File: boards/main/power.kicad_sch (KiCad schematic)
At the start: 19 parts, among them Q1 DMG3415U, U3 RT9080-33GJ5, U4 MCP73831T-2ACI_OT, U5 MAX17048G_T10

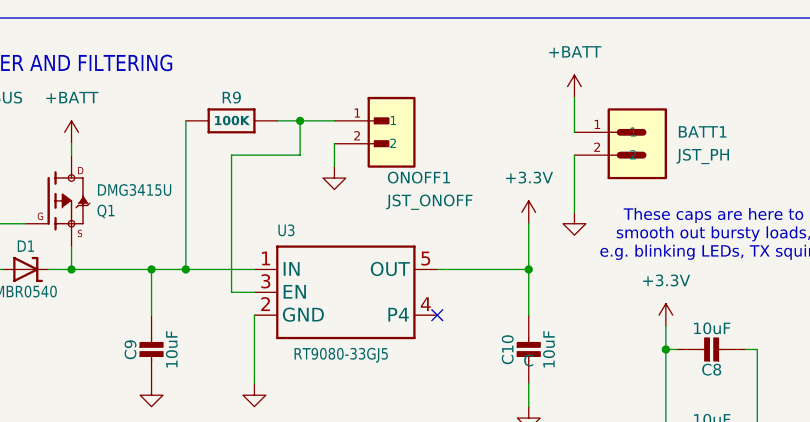
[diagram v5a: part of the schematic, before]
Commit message: Ditch the JST for the buttons, power switch, and haptic motor. Just solder direct
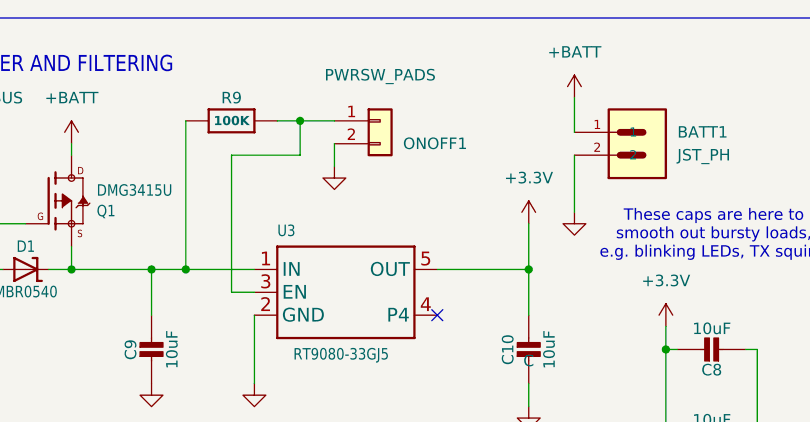
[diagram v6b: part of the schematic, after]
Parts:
- removed ONOFF1: JST_ONOFF, symbol smart_compass_main:SM02B-GHS-TB
- added ONOFF1: PWRSW_PADS, Connector_Wire:SolderWire-0.127sqmm_1x02_P3.7mm_D0.48mm_OD1mm_Relief, symbol Connector_Generic:Conn_01x02
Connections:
- net GND: now also ONOFF1.2 (Pin_2)
- net at R9.2, U3.3 (EN): now also ONOFF1.1 (Pin_1)
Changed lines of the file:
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@@
 	)
 	(symbol
-		(lib_id "smart_compass_main:SM02B-GHS-TB")
-		(at 203.2 41.91 0)
-		(unit 1)
-		(body_style 1)
-		(exclude_from_sim no)
-		(in_bom yes)
-		(on_board yes)
-		(in_pos_files yes)
-		(dnp no)
-		(property "Reference" "ONOFF1"
-			(at 198.882 45.72 0)
-			(show_name no)
-			(do_not_autoplace no)
-			(effects
-				(font
-					(size 1.27 1.27)
-				)
-				(justify left)
-			)
-		)
-		(property "Value" "JST_ONOFF"
-			(at 198.882 48.26 0)
-			(show_name no)
-			(do_not_autoplace no)
-			(effects
-				(font
-					(size 1.27 1.27)
-				)
-				(justify left)
-			)
-		)
-		(property "Footprint" ""
-			(at 203.2 41.91 0)
-			(hide yes)
-			(show_name no)
-			(do_not_autoplace no)
-			(effects
-				(font
-					(size 1.27 1.27)
-				)
-				(justify bottom)
-			)
-		)
-		(property "Datasheet" "https://www.jst-mfg.com/product/pdf/eng/eGH.pdf"
-			(at 203.2 41.91 0)
-			(hide yes)
-			(show_name no)
-			(do_not_autoplace no)
-			(effects
-				(font
-					(size 1.27 1.27)
-				)
-			)
-		)
-		(property "Description" "Connector Header Surface Mount, Right Angle 2 position 0.049 (1.25mm)"
-			(at 203.2 41.91 0)
-			(hide yes)
-			(show_name no)
-			(do_not_autoplace no)
-			(effects
-				(font
-					(size 1.27 1.27)
-				)
-				(justify bottom)
-			)
-		)
-		(property "MF" "JST Sales"
-			(at 203.2 41.91 0)
-			(hide yes)
-			(show_name no)
-			(do_not_autoplace no)
-			(effects
-				(font
-					(size 1.27 1.27)
-				)
-				(justify bottom)
-			)
-		)
-		(property "MP" "SM02B-GHS-TB"
-			(at 203.2 41.91 0)
-			(hide yes)
-			(show_name no)
-			(do_not_autoplace no)
-			(effects
-				(font
-					(size 1.27 1.27)
-				)
-				(justify bottom)
-			)
-		)
-		(property "MANUFACTURER" "JST"
-			(at 203.2 41.91 0)
-			(hide yes)
-			(show_name no)
-			(do_not_autoplace no)
-			(effects
-				(font
-					(size 1.27 1.27)
-				)
-				(justify bottom)
-			)
-		)
-		(property "MPN" "SM02B-GHS-TB"
-			(at 203.2 41.91 0)
-			(hide yes)
-			(show_name no)
-			(do_not_autoplace no)
-			(effects
-				(font
-					(size 1.27 1.27)
-				)
-			)
-		)
-		(property "PRICE" "0.26"
-			(at 203.2 41.91 0)
-			(hide yes)
-			(show_name no)
-			(do_not_autoplace no)
-			(effects
-				(font
-					(size 1.27 1.27)
-				)
-			)
-		)
-		(property "DigiKey_Part_Number" "455-1564-1-ND"
-			(at 203.2 41.91 0)
-			(hide yes)
-			(show_name no)
-			(do_not_autoplace no)
-			(effects
-				(font
-					(size 1.27 1.27)
-				)
-				(justify bottom)
-			)
-		)
-		(property "MAXIMUM_PACKAGE_HIEGHT" ""
-			(at 203.2 41.91 0)
-			(hide yes)
-			(show_name no)
-			(do_not_autoplace no)
-			(effects
-				(font
-					(size 1.27 1.27)
-				)
-			)
-		)
-		(property "Manufacturer" "JST Sales America Inc."
-			(at 203.2 41.91 0)
-			(hide yes)
-			(show_name no)
-			(do_not_autoplace no)
-			(effects
-				(font
-					(size 1.27 1.27)
-				)
-			)
-		)
-		(property "DigiKey_PN" "455-1564-1-ND"
-			(at 203.2 41.91 0)
-			(hide yes)
-			(show_name no)
-			(do_not_autoplace no)
-			(effects
-				(font
-					(size 1.27 1.27)
-				)
-			)
-		)
-		(pin "2"
-		)
-		(pin "1"
-		)
-		(instances
-			(project "SmartCompass"
-				(path "/0c161f28-8075-4403-a867-35208f463636/44fc6246-5945-463a-870f-e1f278c176e3"
-					(reference "ONOFF1")
-					(unit 1)
-				)
-			)
-		)
-	)
-	(symbol
 		(lib_id "power:+BATT")
 		(at 93.98 52.07 0)
@@
 					(unit 1)
 				)
+			)
+		)
+	)
+	(symbol
+		(lib_id "Connector_Generic:Conn_01x02")
+		(at 198.12 39.37 0)
+		(unit 1)
+		(body_style 1)
+		(exclude_from_sim no)
+		(in_bom yes)
+		(on_board yes)
+		(in_pos_files yes)
+		(dnp no)
+		(property "Reference" "ONOFF1"
+			(at 200.66 41.91 0)
+			(show_name no)
+			(do_not_autoplace no)
+			(effects
+				(font
+					(size 1.27 1.27)
+				)
+				(justify left)
+			)
+		)
+		(property "Value" "PWRSW_PADS"
+			(at 198.12 34.29 0)
+			(show_name no)
+			(do_not_autoplace no)
+			(effects
+				(font
+					(size 1.27 1.27)
+				)
+			)
+		)
+		(property "Footprint" "Connector_Wire:SolderWire-0.127sqmm_1x02_P3.7mm_D0.48mm_OD1mm_Relief"
+			(at 198.12 39.37 0)
+			(hide yes)
+			(show_name no)
+			(do_not_autoplace no)
+			(effects
+				(font
+					(size 1.27 1.27)
+				)
+			)
+		)
+		(property "Datasheet" ""
+			(at 198.12 39.37 0)
+			(hide yes)
+			(show_name no)
+			(do_not_autoplace no)
+			(effects
+				(font
+					(size 1.27 1.27)
+				)
+			)
+		)
+		(property "Description" "Soldered wire pads with feed-through strain relief, 2 conductors - case power switch"
+			(at 198.12 39.37 0)
+			(hide yes)
+			(show_name no)
+			(do_not_autoplace no)
+			(effects
+				(font
+					(size 1.27 1.27)
+				)
+			)
+		)
+		(property "MF" "JST Sales"
+			(at 198.12 39.37 0)
+			(hide yes)
+			(show_name no)
+			(do_not_autoplace no)
+			(effects
+				(font
+					(size 1.27 1.27)
+				)
+			)
+		)
+		(property "MP" "SM02B-GHS-TB"
+			(at 198.12 39.37 0)
+			(hide yes)
+			(show_name no)
+			(do_not_autoplace no)
+			(effects
+				(font
+					(size 1.27 1.27)
+				)
+			)
+		)
+		(property "MANUFACTURER" "JST"
+			(at 198.12 39.37 0)
+			(hide yes)
+			(show_name no)
+			(do_not_autoplace no)
+			(effects
+				(font
+					(size 1.27 1.27)
+				)
+			)
+		)
+		(property "MPN" "SM02B-GHS-TB"
+			(at 198.12 39.37 0)
+			(hide yes)
+			(show_name no)
+			(do_not_autoplace no)
+			(effects
+				(font
+					(size 1.27 1.27)
+				)
+			)
+		)
+		(property "DigiKey_Part_Number" "455-1564-1-ND"
+			(at 198.12 39.37 0)
+			(hide yes)
+			(show_name no)
+			(do_not_autoplace no)
+			(effects
+				(font
+					(size 1.27 1.27)
+				)
+			)
+		)
+		(property "MAXIMUM_PACKAGE_HIEGHT" ""
+			(at 198.12 39.37 0)
+			(hide yes)
+			(show_name no)
+			(do_not_autoplace no)
+			(effects
+				(font
+					(size 1.27 1.27)
+				)
+			)
+		)
+		(property "Manufacturer" "JST Sales America Inc."
+			(at 198.12 39.37 0)
+			(hide yes)
+			(show_name no)
+			(do_not_autoplace no)
+			(effects
+				(font
+					(size 1.27 1.27)
+				)
+			)
+		)
+		(property "DigiKey_PN" "455-1564-1-ND"
+			(at 198.12 39.37 0)
+			(hide yes)
+			(show_name no)
+			(do_not_autoplace no)
+			(effects
+				(font
+					(size 1.27 1.27)
+				)
+			)
+		)
+		(property "PRICE" "0.26"
+			(at 198.12 39.37 0)
+			(hide yes)
+			(show_name no)
+			(do_not_autoplace no)
+			(effects
+				(font
+					(size 1.27 1.27)
+				)
+			)
+		)
+		(pin "1"
+		)
+		(pin "2"
+		)
+		(instances
+			(project "SmartCompass"
+				(path "/0c161f28-8075-4403-a867-35208f463636/44fc6246-5945-463a-870f-e1f278c176e3"
+					(reference "ONOFF1")
+					(unit 1)
+				)

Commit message: DMG3415U was superceeded - swap it out and update the docs. Also add another bulk cap to the haptic driver to accommodate the new motor
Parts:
- Q1: value DMG3415U -> DMP2045U; footprint (none) -> Package_TO_SOT_SMD:SOT-23; DigiKey_PN DMG3415UDICT-ND -> DMP2045U-7DICT-ND; MPN DMG3415U-7 -> DMP2045U-7; PRICE 0.48 -> 0.44; Sourcing_Note (none) -> P-channel power mux between the battery and the LDO input: 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
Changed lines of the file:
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@@
 			)
 		)
-		(property "Value" "DMG3415U"
+		(property "Value" "DMP2045U"
 			(at 166.624 46.355 0)
 			(show_name no)
@@
 			)
 		)
-		(property "Footprint" ""
+		(property "Footprint" "Package_TO_SOT_SMD:SOT-23"
 			(at 163.83 48.26 0)
 			(hide yes)
@@
 			)
 		)
-		(property "Datasheet" "https://mm.digikey.com/Volume0/opasdata/d220001/medias/docus/416/DMG3415U.pdf"
+		(property "Datasheet" "https://www.diodes.com/assets/Datasheets/DMP2045U.pdf"
 			(at 163.83 48.26 0)
 			(hide yes)
@@
 			)
 		)
-		(property "MPN" "DMG3415U-7"
+		(property "MPN" "DMP2045U-7"
 			(at 163.83 48.26 0)
 			(hide yes)
@@
 			)
 		)
-		(property "PRICE" "0.48"
+		(property "PRICE" "0.44"
 			(at 163.83 48.26 0)
 			(hide yes)
@@
 			)
 		)
-		(property "DigiKey_PN" "DMG3415UDICT-ND"
+		(property "DigiKey_PN" "DMP2045U-7DICT-ND"
 			(at 163.83 48.26 0)
 			(hide yes)
+			(show_name no)
+			(do_not_autoplace no)
+			(effects
+				(font
+					(size 1.27 1.27)
+				)
+			)
+		)
+		(property "Sourcing_Note" "P-channel power mux between the battery and the LDO input: drain on +BATT, source on the LDO rail, gate on VBUS with a 100k pulldown, paired with the MBR0540 Schottky that feeds the rail from USB. Replaces the DMG3415U-7, which the manufacturer marks NOT RECOMMENDED FOR NEW DESIGN and names this part as its successor. Same SOT-23 package and same G/S/D pinout, so the swap needs no layout change. Package is JEDEC TO-236AB: 2.90 x 1.30mm body, 2.40mm lead span, 0.95mm pitch, which is what Package_TO_SOT_SMD:SOT-23 is drawn for. The earlier footprint, SOT95P240X105-3N, had the same outline but lived in a per-part library that is no longer present, which is why this field had gone empty. Rds(on) is slightly higher than the old part (45mOhm vs 39mOhm at 4.5V drive, 90mOhm vs 71mOhm at 1.8V) and Ciss roughly doubles to 634pF, but neither matters here: the FET carries only the 3.3V LDO input current, a few hundred mA at most, since the LED ring's boost taps +BATT upstream through FB1. Conduction loss is a few mW against an 800mW rating, and the gate time constant through the 100k pulldown is about 60us, far quicker than the VBUS rail decays on unplug."
+			(at 163.83 48.26 0)
+			(hide yes)

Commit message: grab a bunch of datasheets. Fix some models, fix some footprints, replace an unsuited capacitor
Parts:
- BATT1: MANUFACTURER JST -> (none)
- C11: footprint Capacitor_SMD:C_0402_1005Metric -> Capacitor_SMD:C_1206_3216Metric; Dielectric X5R -> X7R; DigiKey_PN 1276-1482-1-ND -> 1276-3179-1-ND; MPN CL05A475MP5NRNC -> CL31B475KBHNFNE; Sourcing_Note (none) -> Bulk capacitor on the battery rail at the charger output. 5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; Tolerance (none) -> 10%; Voltage 10V -> 50V
- C7: footprint Capacitor_SMD:C_0402_1005Metric -> Capacitor_SMD:C_1206_3216Metric; Dielectric X5R -> X7R; DigiKey_PN 1276-1482-1-ND -> 1276-3179-1-ND; MPN CL05A475MP5NRNC -> CL31B475KBHNFNE; Sourcing_Note (none) -> Bulk capacitor on the USB VBUS rail at the charger input. 5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; Tolerance (none) -> 10%; Voltage 10V -> 50V
- ONOFF1: DigiKey_PN 455-1564-1-ND -> (none); DigiKey_Part_Number 455-1564-1-ND -> (none); MANUFACTURER JST -> (none); MF JST Sales -> (none); MP SM02B-GHS-TB -> (none); MPN SM02B-GHS-TB -> (none); Manufacturer JST Sales America Inc. -> (none); PRICE 0.26 -> (none)
